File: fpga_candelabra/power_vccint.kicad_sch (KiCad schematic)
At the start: 104 parts, among them U2 TPS53667, U3 CSD95491Q5MC, U4 CSD95491Q5MC, U5 CSD95491Q5MC, U6 CSD95491Q5MC

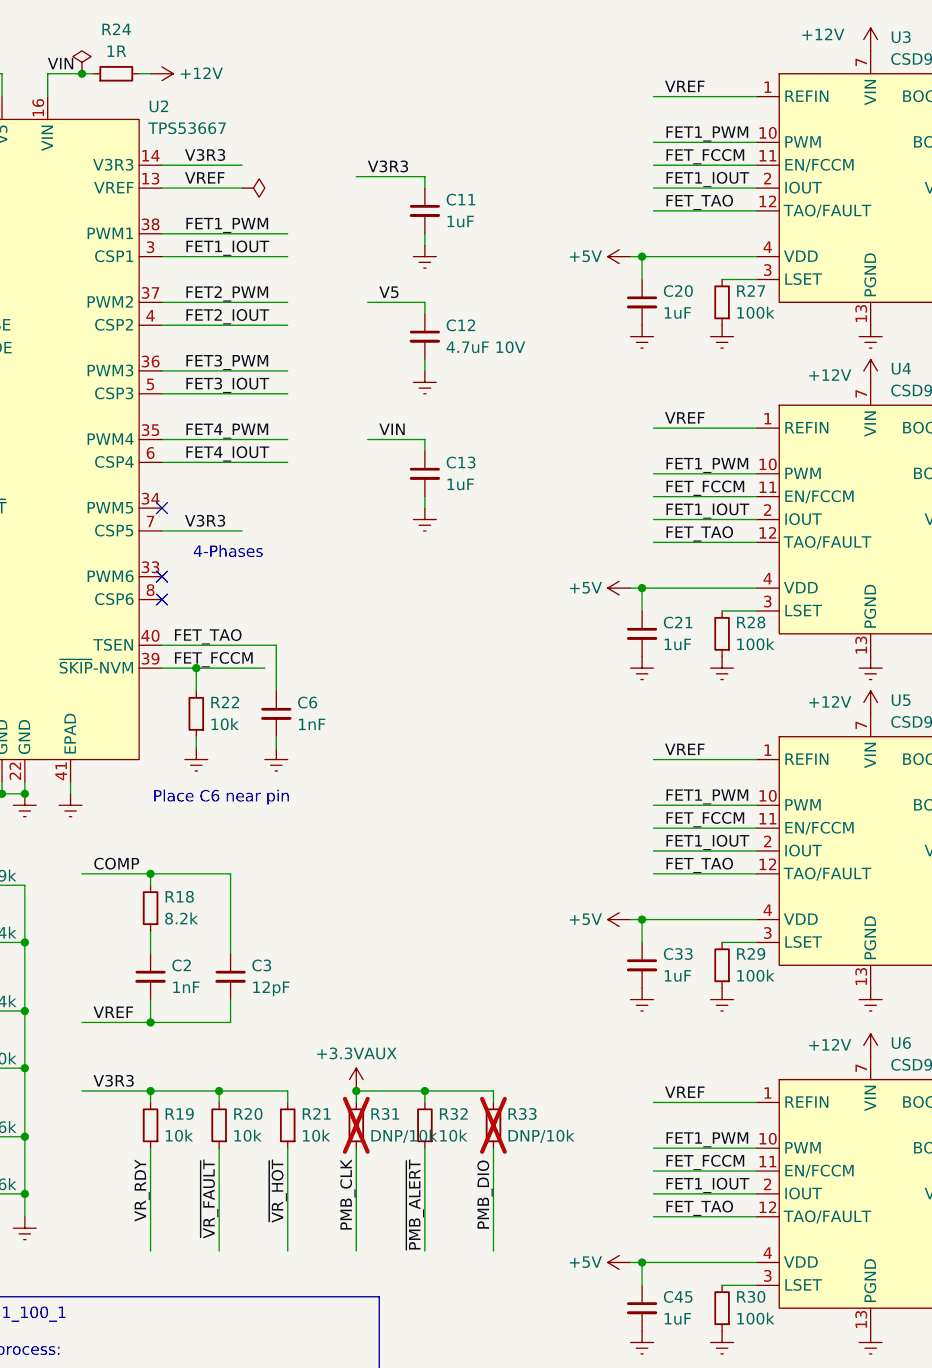
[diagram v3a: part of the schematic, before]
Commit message: candelabra: add i-pex extension ports, remove FMC1
* update bank/mgt allocation
* add basic pcb floorplanning

Signed-off-by: Yichuan Gao <gaoyichuan000@gmail.com>
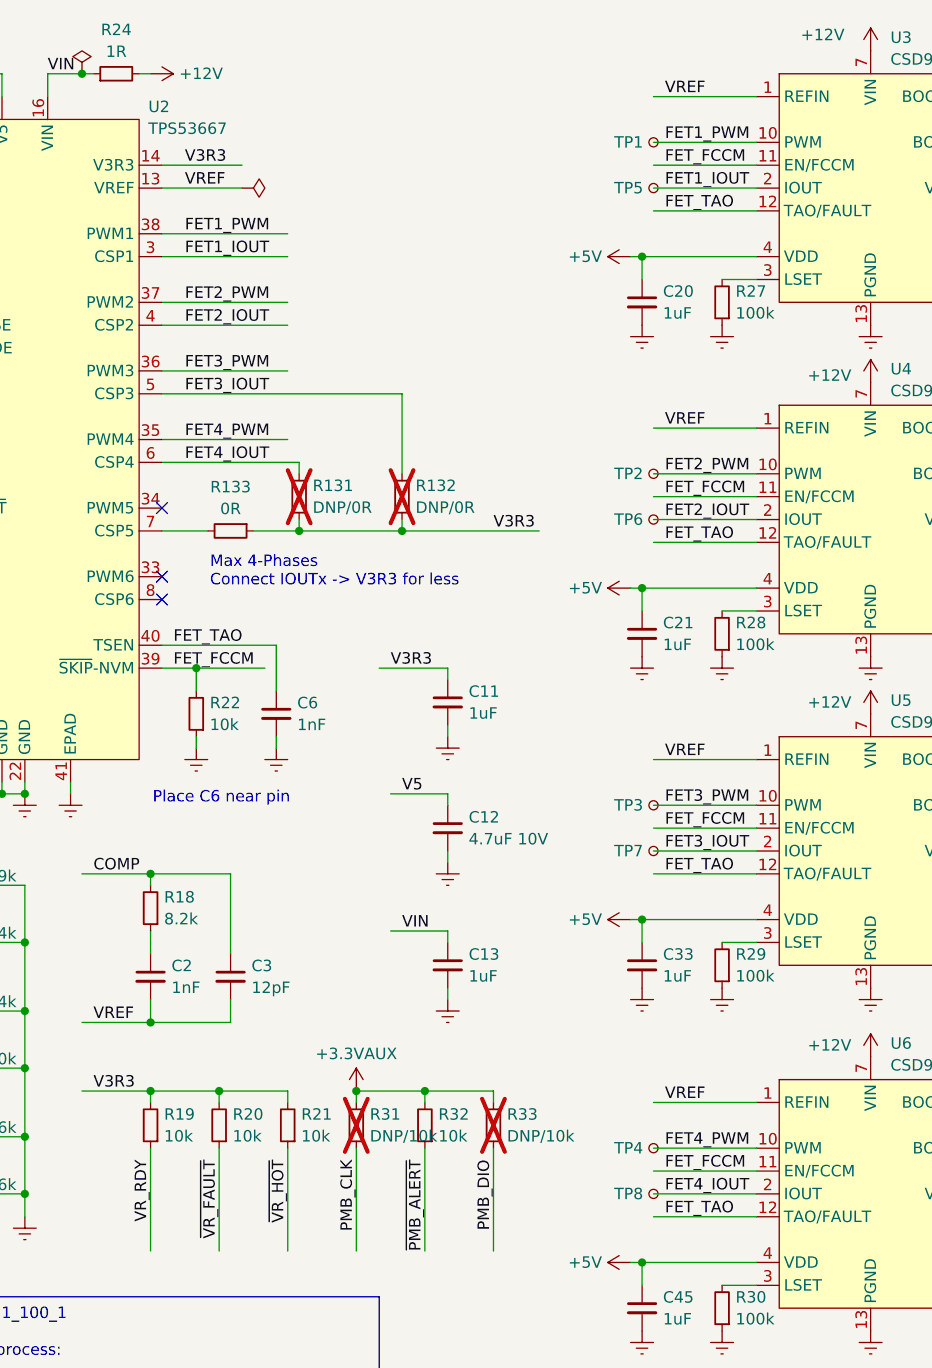
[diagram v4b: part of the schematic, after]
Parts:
- added R131, R132: DNP/0R, Resistor_SMD:R_0402_1005Metric, symbol Device:R_Small
- added R133: 0R, Resistor_SMD:R_0402_1005Metric, symbol Device:R_Small
- added TP1, TP2, TP3, TP4, TP5, TP6, TP7, TP8: TestPoint_Small, TestPoint:TestPoint_Pad_D1.0mm, symbol Connector:TestPoint_Small
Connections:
- net FET1_IOUT: now also TP5.1; no longer U4.2 (IOUT), U5.2 (IOUT), U6.2 (IOUT)
- net FET1_PWM: now also TP1.1; no longer U4.10 (PWM), U5.10 (PWM), U6.10 (PWM)
- net FET2_IOUT: now also U4.2 (IOUT), TP6.1
- net FET2_PWM: now also U4.10 (PWM), TP2.1
- net FET3_IOUT: now also U5.2 (IOUT), R132.2, TP7.1
- net FET3_PWM: now also U5.10 (PWM), TP3.1
- net FET4_IOUT: now also U6.2 (IOUT), R131.2, TP8.1
- net FET4_PWM: now also U6.10 (PWM), TP4.1
- net V3R3: now also R131.1, R132.1, R133.1; no longer U2.7 (CSP5)
- new net: R133.2, U2.7 (CSP5)
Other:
- note added: "Max 4-Phases Connect IOUTx -> V3R3 for less"
- note removed: "4-Phases"
- moved on the sheet: C11, C12, C13

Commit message: fpga_candelabra: major revision
* Finish DDR4 & QSFP+ & PCIe layout
* Change FMC to LPC
* Add mikroBUS extension
* 12V input & PDN updates
* FPGA config updates

Signed-off-by: Yichuan Gao <gaoyichuan000@gmail.com>
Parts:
- L1, L2, L3, L4: value SMIS130804-R15MT -> VLBU1007090T-R15L; footprint CHIPSAlliance_Inductor_SMD:L_SXN_SMIS130804 -> CHIPSAlliance_Inductor_SMD:L_TDK_VLBU1007090; LCSC Part C389943 -> C2045227; Manufacturer SXN(顺翔诺) -> TDK
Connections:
- net +12V renamed +12V_G1
- net VSN renamed VS-
- net VSP renamed VS+
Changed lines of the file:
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@@
 		)
 	)
-	(label "VSP"
+	(label "VS+"
 		(at 270.51 93.98 0)
 		(fields_autoplaced yes)
@@
 		)
 	)
-	(label "VSN"
+	(label "VS-"
 		(at 46.99 30.48 0)
 		(fields_autoplaced yes)
@@
 		)
 	)
-	(label "VSN"
+	(label "VS-"
 		(at 270.51 101.6 0)
 		(fields_autoplaced yes)
@@
 		)
 	)
-	(label "VSP"
+	(label "VS+"
 		(at 46.99 27.94 0)
 		(fields_autoplaced yes)
@@
 			)
 		)
-		(property "Value" "+12V"
+		(property "Value" "+12V_G1"
 			(at 84.455 20.32 90)
 			(effects
@@
 			)
 		)
-		(property "Value" "SMIS130804-R15MT"
+		(property "Value" "VLBU1007090T-R15L"
 			(at 185.42 78.9474 90)
 			(effects
@@
 			)
 		)
-		(property "Footprint" "CHIPSAlliance_Inductor_SMD:L_SXN_SMIS130804"
+		(property "Footprint" "CHIPSAlliance_Inductor_SMD:L_TDK_VLBU1007090"
 			(at 185.42 74.93 0)
 			(effects
@@
 			)
 		)
-		(property "Datasheet" "https://atta.szlcsc.com/upload/public/pdf/source/20210810/C89E6F775779B79874D7B6E709D70FFB.pdf"
+		(property "Datasheet" "https://product.tdk.com/system/files/dam/doc/product/inductor/inductor/smd/catalog/inductor_commercial_power_vlbu1007090_en.pdf"
 			(at 185.42 74.93 0)
 			(effects
@@
 			)
 		)
-		(property "Description" "150nH 45A / 85A"
+		(property "Description" "150nH 70A / 90A"
 			(at 185.42 74.93 0)
 			(effects
@@
 			)
 		)
-		(property "LCSC Part" "C389943"
+		(property "LCSC Part" "C2045227"
 			(at 185.42 74.93 90)
 			(effects
@@
 			)
 		)
-		(property "Manufacturer" "SXN(顺翔诺)"
+		(property "Manufacturer" "TDK"
 			(at 185.42 74.93 90)
 			(effects
@@
 		(on_board yes)
 		(dnp no)
+		(fields_autoplaced yes)
 		(property "Reference" "#PWR031"
 			(at 161.29 58.42 0)
@@
 			)
 		)
-		(property "Value" "+12V"
-			(at 156.718 53.848 0)
+		(property "Value" "+12V_G1"
+			(at 159.8931 53.34 0)
 			(effects
 				(font
 					(size 1.27 1.27)
 				)
+				(justify right)
 			)
 		)
@@
 			)
 		)
-		(property "Value" "+12V"
+		(property "Value" "+12V_G1"
 			(at 203.2 54.2869 0)
 			(effects
@@
 			)
 		)
-		(property "Value" "SMIS130804-R15MT"
+		(property "Value" "VLBU1007090T-R15L"
 			(at 185.42 42.1174 90)
 			(effects
@@
 			)
 		)
-		(property "Footprint" "CHIPSAlliance_Inductor_SMD:L_SXN_SMIS130804"
+		(property "Footprint" "CHIPSAlliance_Inductor_SMD:L_TDK_VLBU1007090"
 			(at 185.42 38.1 0)
 			(effects
@@
 			)
 		)
-		(property "Datasheet" "https://atta.szlcsc.com/upload/public/pdf/source/20210810/C89E6F775779B79874D7B6E709D70FFB.pdf"
+		(property "Datasheet" "https://product.tdk.com/system/files/dam/doc/product/inductor/inductor/smd/catalog/inductor_commercial_power_vlbu1007090_en.pdf"
 			(at 185.42 38.1 0)
 			(effects
@@
 			)
 		)
-		(property "Description" "150nH 45A / 85A"
+		(property "Description" "150nH 70A / 90A"
 			(at 185.42 38.1 0)
 			(effects
@@
 			)
 		)
-		(property "LCSC Part" "C389943"
+		(property "LCSC Part" "C2045227"
 			(at 185.42 38.1 90)
 			(effects
@@
 			)
 		)
-		(property "Manufacturer" "SXN(顺翔诺)"
+		(property "Manufacturer" "TDK"
 			(at 185.42 38.1 90)
 			(effects
@@
 			)
 		)
-		(property "Value" "+12V"
+		(property "Value" "+12V_G1"
 			(at 203.2 91.186 0)
 			(effects
@@
 			)
 		)
-		(property "Value" "+12V"
+		(property "Value" "+12V_G1"
 			(at 203.2 17.4569 0)
 			(effects
@@
 			)
 		)
-		(property "Value" "SMIS130804-R15MT"
+		(property "Value" "VLBU1007090T-R15L"
 			(at 185.42 115.7774 90)
 			(effects
@@
 			)
 		)
-		(property "Footprint" "CHIPSAlliance_Inductor_SMD:L_SXN_SMIS130804"
+		(property "Footprint" "CHIPSAlliance_Inductor_SMD:L_TDK_VLBU1007090"
 			(at 185.42 111.76 0)
 			(effects
@@
 			)
 		)
-		(property "Datasheet" "https://atta.szlcsc.com/upload/public/pdf/source/20210810/C89E6F775779B79874D7B6E709D70FFB.pdf"
+		(property "Datasheet" "https://product.tdk.com/system/files/dam/doc/product/inductor/inductor/smd/catalog/inductor_commercial_power_vlbu1007090_en.pdf"
 			(at 185.42 111.76 0)
 			(effects
@@
 			)
 		)
-		(property "Description" "150nH 45A / 85A"
+		(property "Description" "150nH 70A / 90A"
 			(at 185.42 111.76 0)
 			(effects
@@
 			)
 		)
-		(property "LCSC Part" "C389943"
+		(property "LCSC Part" "C2045227"
 			(at 185.42 111.76 90)
 			(effects
@@
 			)
 		)
-		(property "Manufacturer" "SXN(顺翔诺)"
+		(property "Manufacturer" "TDK"
 			(at 185.42 111.76 90)
 			(effects
@@
 			)
 		)
-		(property "Value" "+12V"
-			(at 155.956 16.002 0)
+		(property "Value" "+12V_G1"
+			(at 155.448 16.51 0)
 			(effects
 				(font
@@
 		(on_board yes)
 		(dnp no)
+		(fields_autoplaced yes)
 		(property "Reference" "#PWR045"
 			(at 161.29 95.25 0)
@@
 			)
 		)
-		(property "Value" "+12V"
-			(at 156.718 90.17 0)
+		(property "Value" "+12V_G1"
+			(at 159.8931 90.17 0)
 			(effects
 				(font
 					(size 1.27 1.27)
 				)
+				(justify right)
 			)
 		)
@@
 			)
 		)
-		(property "Value" "SMIS130804-R15MT"
+		(property "Value" "VLBU1007090T-R15L"
 			(at 185.42 153.8774 90)
 			(effects
@@
 			)
 		)
-		(property "Footprint" "CHIPSAlliance_Inductor_SMD:L_SXN_SMIS130804"
+		(property "Footprint" "CHIPSAlliance_Inductor_SMD:L_TDK_VLBU1007090"
 			(at 185.42 149.86 0)
 			(effects
@@
 			)
 		)
-		(property "Datasheet" "https://atta.szlcsc.com/upload/public/pdf/source/20210810/C89E6F775779B79874D7B6E709D70FFB.pdf"
+		(property "Datasheet" "https://product.tdk.com/system/files/dam/doc/product/inductor/inductor/smd/catalog/inductor_commercial_power_vlbu1007090_en.pdf"
 			(at 185.42 149.86 0)
 			(effects
@@
 			)
 		)
-		(property "Description" "150nH 45A / 85A"
+		(property "Description" "150nH 70A / 90A"
 			(at 185.42 149.86 0)
 			(effects
@@
 			)
 		)
-		(property "LCSC Part" "C389943"
+		(property "LCSC Part" "C2045227"
 			(at 185.42 149.86 90)
 			(effects
@@
 			)
 		)
-		(property "Manufacturer" "SXN(顺翔诺)"
+		(property "Manufacturer" "TDK"
 			(at 185.42 149.86 90)
 			(effects
@@
 		(on_board yes)
 		(dnp no)
+		(fields_autoplaced yes)
 		(property "Reference" "#PWR059"
 			(at 161.29 133.35 0)
@@
 			)
 		)
-		(property "Value" "+12V"
-			(at 156.718 128.27 0)
+		(property "Value" "+12V_G1"
+			(at 159.8931 128.27 0)
 			(effects
 				(font
 					(size 1.27 1.27)
 				)
+				(justify right)
 			)
 		)
@@
 			)
 		)
-		(property "Value" "+12V"
+		(property "Value" "+12V_G1"
 			(at 203.2 129.2169 0)
 			(effects

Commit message: fpga_candelabra: sch & layout v0.5, pass basic ERC & DRC
Signed-off-by: Yichuan Gao <gaoyichuan000@gmail.com>
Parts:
- TP1, TP2, TP3, TP4, TP5, TP6, TP7, TP8: now left out of the parts list
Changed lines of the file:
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@@
 		(unit 1)
 		(exclude_from_sim no)
-		(in_bom yes)
+		(in_bom no)
 		(on_board yes)
 		(dnp no)
@@
 		(unit 1)
 		(exclude_from_sim no)
-		(in_bom yes)
+		(in_bom no)
 		(on_board yes)
 		(dnp no)
@@
 		(unit 1)
 		(exclude_from_sim no)
-		(in_bom yes)
+		(in_bom no)
 		(on_board yes)
 		(dnp no)
@@
 		(unit 1)
 		(exclude_from_sim no)
-		(in_bom yes)
+		(in_bom no)
 		(on_board yes)
 		(dnp no)
@@
 		(unit 1)
 		(exclude_from_sim no)
-		(in_bom yes)
+		(in_bom no)
 		(on_board yes)
 		(dnp no)
@@
 		(unit 1)
 		(exclude_from_sim no)
-		(in_bom yes)
+		(in_bom no)
 		(on_board yes)
 		(dnp no)
@@
 		(unit 1)
 		(exclude_from_sim no)
-		(in_bom yes)
+		(in_bom no)
 		(on_board yes)
 		(dnp no)
@@
 	)
 	(symbol
-		(lib_id "CHIPSAlliance_Power:PWR_FLAG")
-		(at 91.44 33.02 270)
-		(unit 1)
-		(exclude_from_sim no)
-		(in_bom yes)
-		(on_board yes)
-		(dnp no)
-		(fields_autoplaced yes)
-		(property "Reference" "#FLG04"
-			(at 93.345 33.02 0)
-			(effects
-				(font
-					(size 1.27 1.27)
-				)
-				(hide yes)
-			)
-		)
-		(property "Value" "PWR_FLAG"
-			(at 95.5731 33.02 0)
-			(effects
-				(font
-					(size 1.27 1.27)
-				)
-				(hide yes)
-			)
-		)
-		(property "Footprint" ""
-			(at 91.44 33.02 0)
-			(effects
-				(font
-					(size 1.27 1.27)
-				)
-				(hide yes)
-			)
-		)
-		(property "Datasheet" "~"
-			(at 91.44 33.02 0)
-			(effects
-				(font
-					(size 1.27 1.27)
-				)
-				(hide yes)
-			)
-		)
-		(property "Description" "Special symbol for telling ERC where power comes from"
-			(at 91.44 33.02 0)
-			(effects
-				(font
-					(size 1.27 1.27)
-				)
-				(hide yes)
-			)
-		)
-		(pin "1"
-		)
-		(instances
-			(project "fpga_candelabra"
-				(path "/01ed9e92-4e50-4b41-90dc-10444aaec5f7/beaa4e74-1d18-44b4-b7c5-122d2a26ede8"
-					(reference "#FLG04")
-					(unit 1)
-				)
-			)
-		)
-	)
-	(symbol
 		(lib_id "power:Earth")
 		(at 208.28 119.38 0)
@@
 		(unit 1)
 		(exclude_from_sim no)
-		(in_bom yes)
+		(in_bom no)
 		(on_board yes)
 		(dnp no)

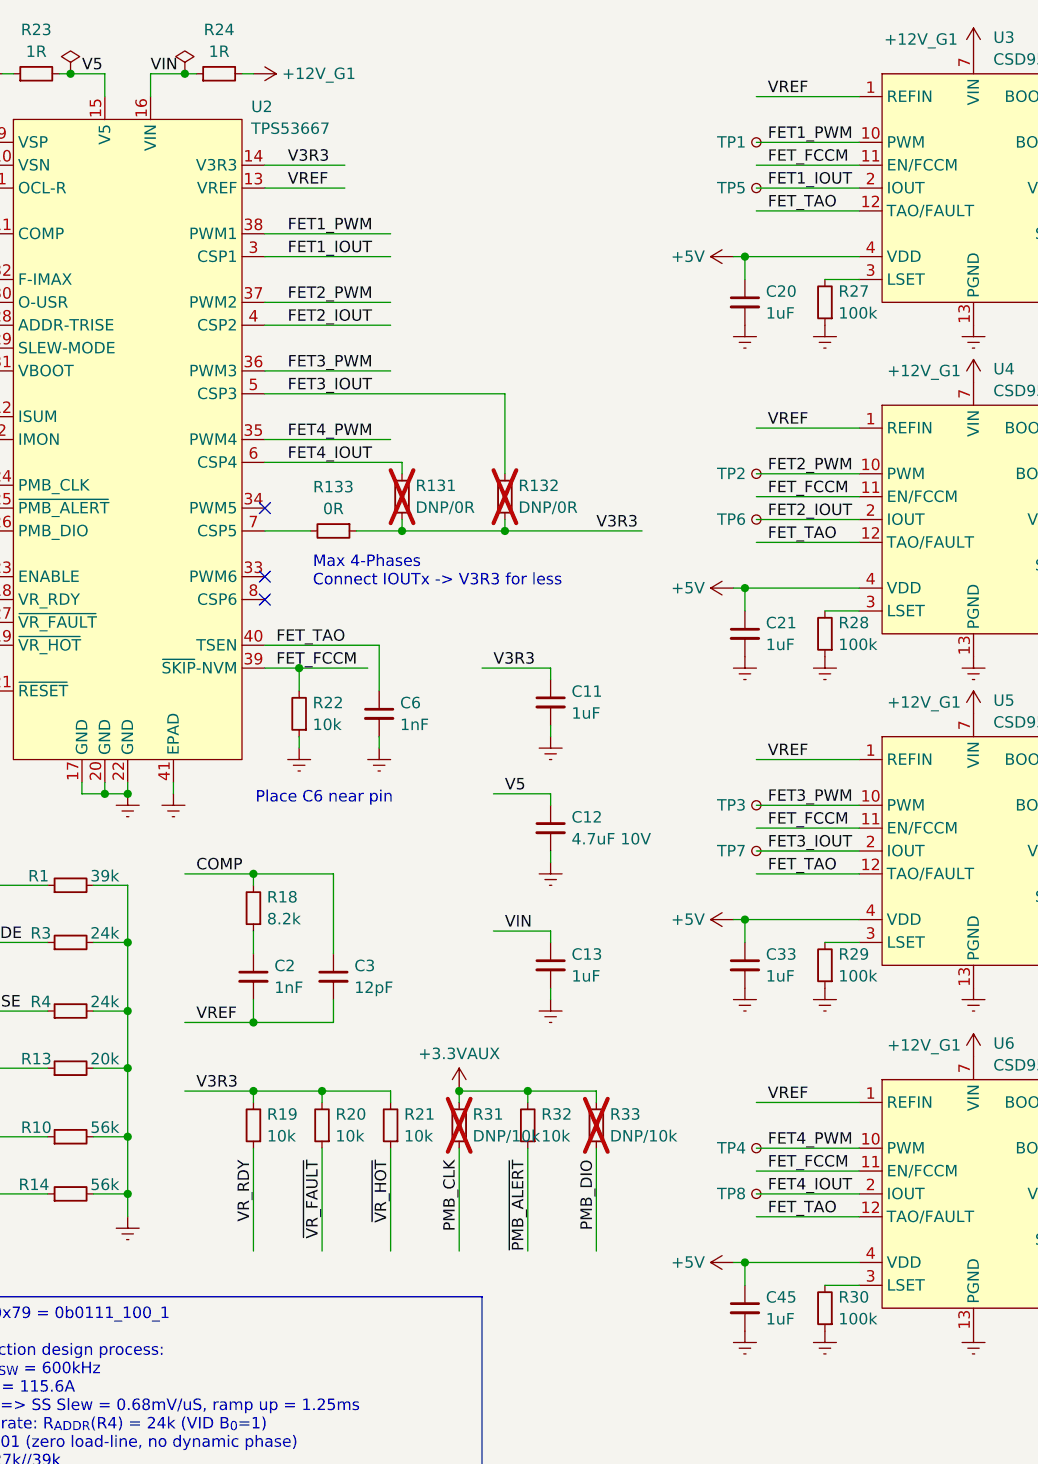
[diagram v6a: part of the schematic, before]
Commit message: fpga_candelabra: first rev fixes - fix vccint power stage FCCM mode - add ddr4 vref decoupling cap - refactor status LEDs - minor layout changes
Signed-off-by: Yichuan Gao <gaoyichuan000@gmail.com>
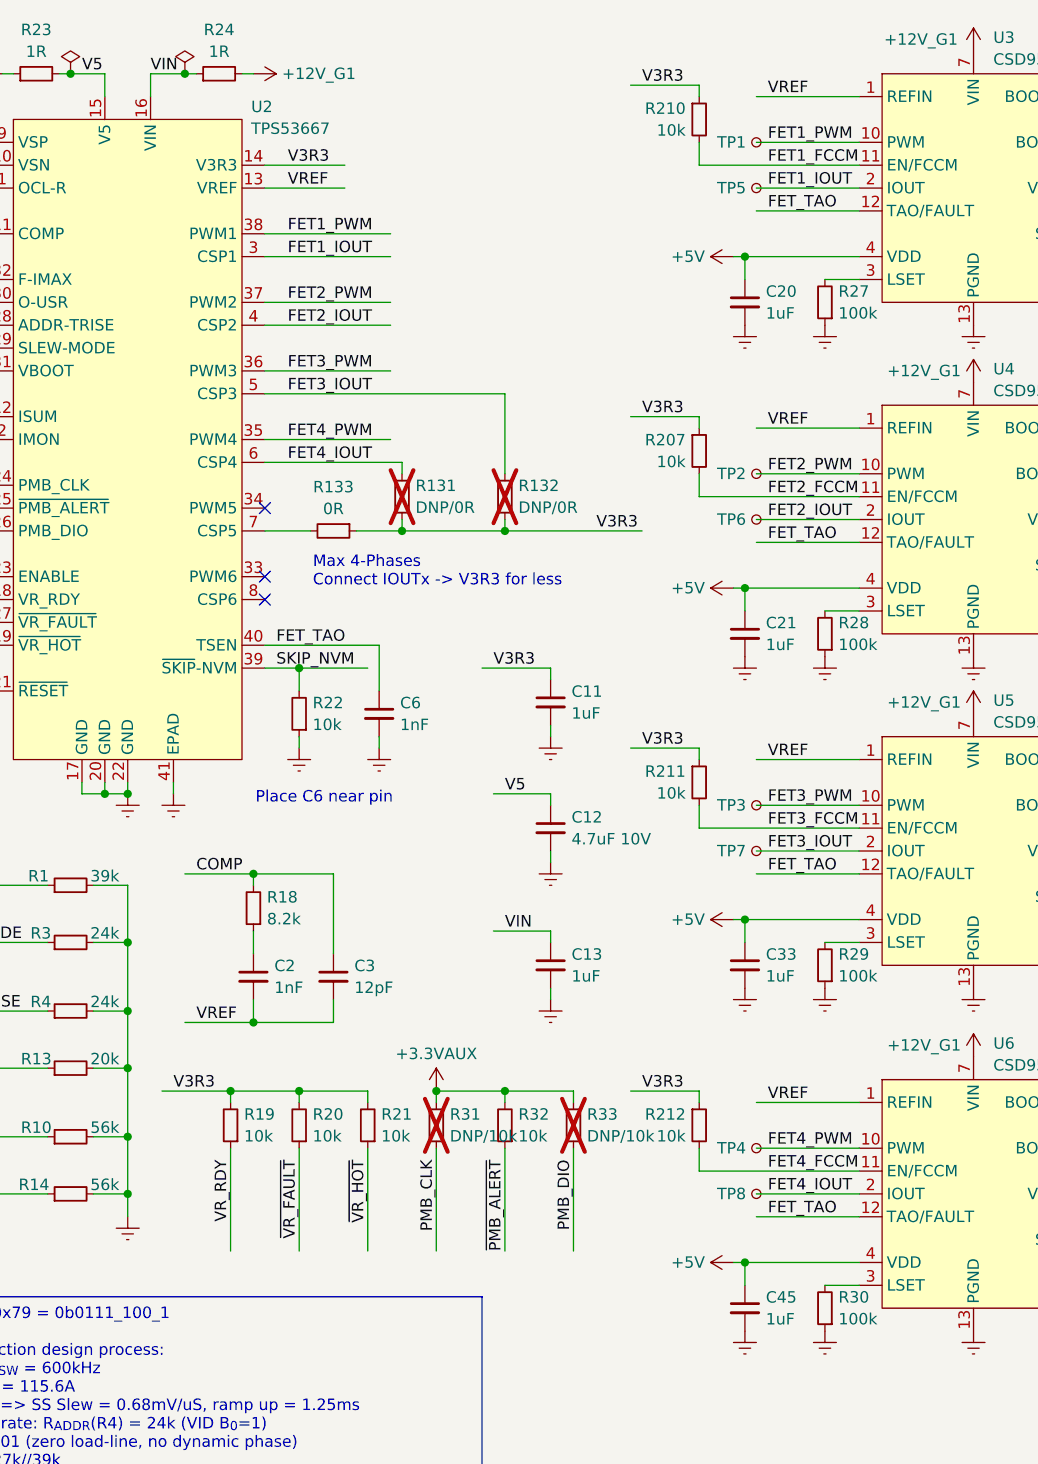
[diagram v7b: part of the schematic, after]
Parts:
- added R207, R210, R211, R212: 10k, Resistor_SMD:R_0402_1005Metric, symbol Device:R_Small
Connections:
- net V3R3: now also R207.1, R210.1, R211.1, R212.1
- removed net FET_FCCM: R22.2, U2.39 (~{SKIP}-NVM), U3.11 (EN/FCCM), U4.11 (EN/FCCM), U5.11 (EN/FCCM), U6.11 (EN/FCCM)
- new net FET1_FCCM: R210.2, U3.11 (EN/FCCM)
- new net FET2_FCCM: R207.2, U4.11 (EN/FCCM)
- new net FET3_FCCM: R211.2, U5.11 (EN/FCCM)
- new net FET4_FCCM: R212.2, U6.11 (EN/FCCM)
- new net SKIP_NVM: R22.2, U2.39 (~{SKIP}-NVM)
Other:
- moved on the sheet: R19, R20, R21, R31, R32, R33

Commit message: fpga_candelabra: more bugfixes & improvements for rev 0.2.0
- Add Digilent JTAG-SMT2-NC onboard
- Add fan controller & 4pin fan header
- Use 9pin header for USB2.0
- Misc fixes for structure

Signed-off-by: Yichuan Gao <gaoyichuan000@gmail.com>
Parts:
- C57, C58, C59, C60: LCSC Part (none) -> C424362
